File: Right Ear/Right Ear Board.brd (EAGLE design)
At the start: 157.5 x 20.3 mm, 6 parts, among them J1 502585-0470

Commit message: Update right ear boards
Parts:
- removed C2: (no value), rcl:C0402
- added C4: 10uF, rcl:C0603K
- added SV2, SV3: (no value), con-lstb:MA03-1
- C1: value (none) -> 10uF; device rcl:C0402 -> rcl:C0603K
- moved C1 146.6 mm to (3.43, 18.2)
- moved LED7 118.7 mm to (31.8, 16.5), turned to 180 degrees
- moved LED1 7.73 mm to (8.89, 16.5), turned to 180 degrees
- moved SV1 6.93 mm to (9.14, 3.05), flipped to the top, turned to 0 degrees
- moved J1 2.84 mm to (6.35, 11.4), turned to 270 degrees
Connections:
- removed net N$1: LED1.2-DOUT, LED7.4-DIN
- new net DATA: LED1.2-DOUT, LED7.4-DIN, SV2.2, SV3.2
- net +5V: now also C4.1, SV2.1, SV3.3; no longer C2.1
- net GND: now also C4.2, SV2.3, SV3.1; no longer C2.2
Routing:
- net N$1: track 157.1 -> 0.00 mm
- net +5V: track 186.5 -> 50.9 mm
- net GND: track 6.75 -> 61.3 mm, vias 1 -> 2
- net DATA: track 0.00 -> 33.5 mm, vias 0 -> 3
- net DI: track 7.05 -> 16.3 mm
- net SERVO_PWM: track 14.9 -> 12.8 mm, vias 0 -> 1
- removed copper zone on layer 1, net GND
- removed copper zone on layer 16, net GND
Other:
- board size 157.5 x 20.3 mm -> 39.4 x 20.3 mm

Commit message: Made changes
Change LED caps to .1uF on right ear and center
Add resistor to D2
Add level shifters (1 for D1, 1 for D2)
Add mount holes on right ear
Add mosfet for servo (see things to consider.txt)
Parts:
- C1, C4: value 10uF -> .1uF
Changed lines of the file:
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@@
 <?xml version="1.0" encoding="utf-8"?>
 <!DOCTYPE eagle SYSTEM "eagle.dtd">
-<eagle version="8.5.0">
+<eagle version="8.3.1">
 <drawing>
 <settings>
@@
 <param name="dpMaxLengthDifference" value="10mm"/>
 <param name="dpGapFactor" value="2.5"/>
+<param name="checkGrid" value="0"/>
 <param name="checkAngle" value="0"/>
 <param name="checkFont" value="1"/>
 <param name="checkRestrict" value="1"/>
-<param name="checkStop" value="0"/>
-<param name="checkValues" value="0"/>
 <param name="useDiameter" value="13"/>
 <param name="maxErrors" value="50"/>
@@
 <attribute name="VALUE" x="18.161" y="7.62" size="1.27" layer="27" ratio="10" rot="R90"/>
 </element>
-<element name="C4" library="rcl" package="C0603K" value="10uF" x="25.4" y="18.161" smashed="yes" rot="R180">
+<element name="C4" library="rcl" package="C0603K" value=".1uF" x="25.4" y="18.161" smashed="yes" rot="R180">
 <attribute name="NAME" x="26.2" y="17.511" size="1.016" layer="25" rot="R180"/>
 <attribute name="PARTNO" value="GRM188R61A106KE69D" x="25.4" y="18.161" size="1.778" layer="27" rot="R180" display="off"/>
 </element>
-<element name="C1" library="rcl" package="C0603K" value="10uF" x="3.429" y="18.161" smashed="yes" rot="R180">
+<element name="C1" library="rcl" package="C0603K" value=".1uF" x="3.429" y="18.161" smashed="yes" rot="R180">
 <attribute name="NAME" x="4.229" y="17.511" size="1.016" layer="25" rot="R180"/>
 <attribute name="PARTNO" value="GRM188R61A106KE69D" x="3.429" y="18.161" size="1.778" layer="27" rot="R180" display="off"/>

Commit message: Redid right ear board layouts
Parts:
- moved SV1 13.0 mm to (21.6, 6.73), turned to 90 degrees
- moved C1 11.8 mm to (14.4, 13.6), turned to 0 degrees
- moved LED1 8.98 mm to (15.2, 10.2)
- moved C4 8.82 mm to (33.5, 14.7), turned to 0 degrees
- moved LED7 7.04 mm to (34.8, 10.2)
- moved SV3 6.71 mm to (21.6, 13.6)
- moved SV2 5.33 mm to (29.3, 10.3)
- moved J1 1.27 mm to (6.35, 10.2), flipped to the top, turned to 90 degrees
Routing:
- net GND: track 61.3 -> 46.7 mm, vias 2 -> 4
- net DATA: track 33.5 -> 19.4 mm, vias 3 -> 0
- net SERVO_PWM: track 12.8 -> 21.9 mm, vias 1 -> 2
- net +5V: track 50.9 -> 47.3 mm, vias 1 -> 2
- net DI: track 16.3 -> 15.4 mm, vias 1 -> 0
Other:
- board size 39.4 x 20.3 mm -> 40.6 x 20.3 mm

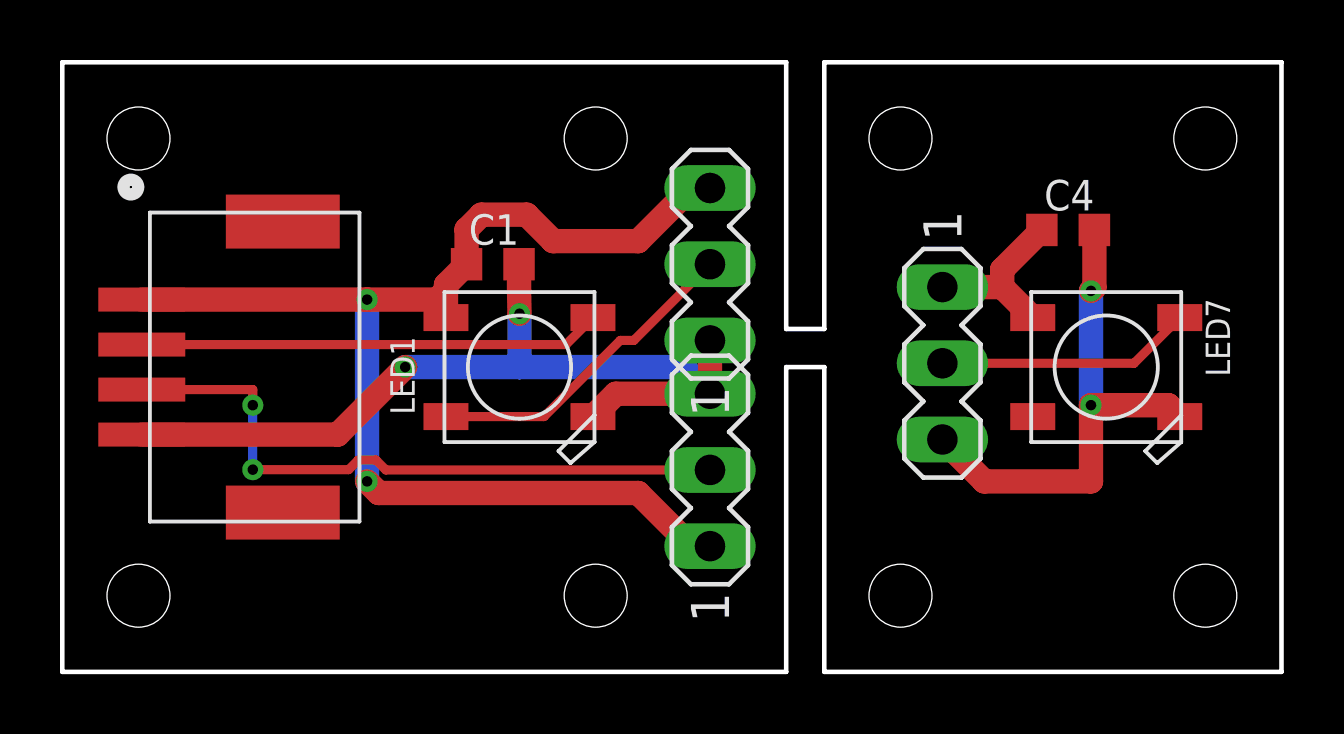
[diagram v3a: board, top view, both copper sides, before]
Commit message: Added level shifter to center dash
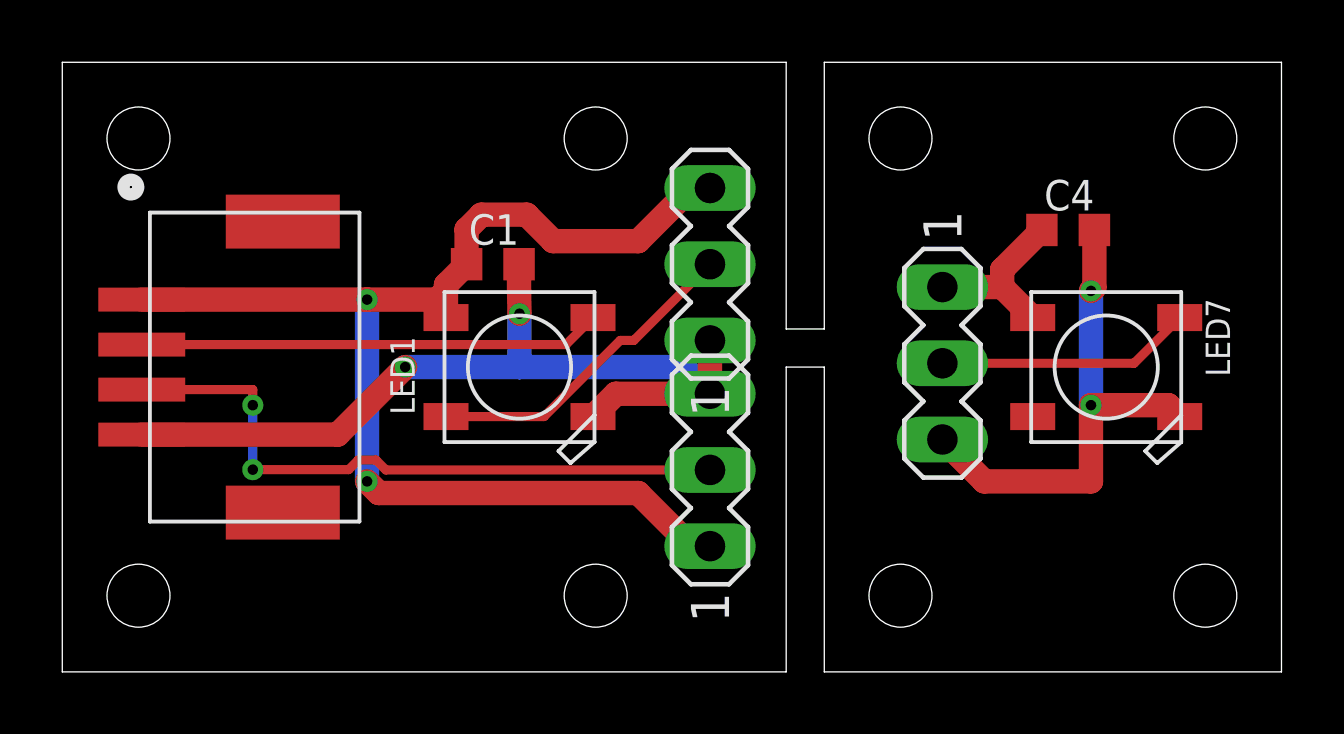
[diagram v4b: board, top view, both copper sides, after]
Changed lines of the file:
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@@
 <setting verticaltext="up"/>
 </settings>
-<grid distance="50" unitdist="mil" unit="mm" style="lines" multiple="1" display="no" altdistance="5" altunitdist="mil" altunit="inch"/>
+<grid distance="50" unitdist="mil" unit="inch" style="lines" multiple="1" display="no" altdistance="5" altunitdist="mil" altunit="inch"/>
 <layers>
 <layer number="1" name="Top" color="4" fill="1" visible="yes" active="yes"/>
@@
 <board>
 <plain>
-<wire x1="40.64" y1="0" x2="40.64" y2="20.32" width="0.1524" layer="20"/>
-<wire x1="0" y1="20.32" x2="0" y2="0" width="0.1524" layer="20"/>
-<wire x1="24.13" y1="11.43" x2="25.4" y2="11.43" width="0.1524" layer="20"/>
-<wire x1="24.13" y1="10.16" x2="25.4" y2="10.16" width="0.1524" layer="20"/>
-<wire x1="0" y1="20.32" x2="24.13" y2="20.32" width="0.1524" layer="20"/>
-<wire x1="24.13" y1="20.32" x2="24.13" y2="11.43" width="0.1524" layer="20"/>
-<wire x1="25.4" y1="11.43" x2="25.4" y2="20.32" width="0.1524" layer="20"/>
-<wire x1="25.4" y1="20.32" x2="40.64" y2="20.32" width="0.1524" layer="20"/>
-<wire x1="25.4" y1="10.16" x2="25.4" y2="0" width="0.1524" layer="20"/>
-<wire x1="25.4" y1="0" x2="40.64" y2="0" width="0.1524" layer="20"/>
-<wire x1="24.13" y1="10.16" x2="24.13" y2="0" width="0.1524" layer="20"/>
-<wire x1="24.13" y1="0" x2="0" y2="0" width="0.1524" layer="20"/>
+<wire x1="40.64" y1="0" x2="40.64" y2="20.32" width="0" layer="20"/>
+<wire x1="0" y1="20.32" x2="0" y2="0" width="0" layer="20"/>
+<wire x1="24.13" y1="11.43" x2="25.4" y2="11.43" width="0" layer="20"/>
+<wire x1="24.13" y1="10.16" x2="25.4" y2="10.16" width="0" layer="20"/>
+<wire x1="0" y1="20.32" x2="24.13" y2="20.32" width="0" layer="20"/>
+<wire x1="24.13" y1="20.32" x2="24.13" y2="11.43" width="0" layer="20"/>
+<wire x1="25.4" y1="11.43" x2="25.4" y2="20.32" width="0" layer="20"/>
+<wire x1="25.4" y1="20.32" x2="40.64" y2="20.32" width="0" layer="20"/>
+<wire x1="25.4" y1="10.16" x2="25.4" y2="0" width="0" layer="20"/>
+<wire x1="25.4" y1="0" x2="40.64" y2="0" width="0" layer="20"/>
+<wire x1="24.13" y1="10.16" x2="24.13" y2="0" width="0" layer="20"/>
+<wire x1="24.13" y1="0" x2="0" y2="0" width="0" layer="20"/>
 <hole x="2.54" y="17.78" drill="2.1"/>
 <hole x="2.54" y="2.54" drill="2.1"/>

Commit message: Done with board layouts
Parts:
- moved LED1 10.2 mm to (5.08, 10.2)
- moved C1 9.79 mm to (4.57, 14.1)
- moved J1 7.75 mm to (14.1, 10.2), turned to 270 degrees
- moved C4 1.27 mm to (34.8, 14.7)
- moved LED7 0.76 mm to (35.6, 10.2)
- moved SV3 0.63 mm to (22.1, 14.0)
- moved SV1 0.51 mm to (22.1, 6.73)
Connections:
- net +5V: now also SV1.2; no longer SV1.1
- net SERVO_PWM: now also SV1.1; no longer SV1.2
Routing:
- net DATA: track 19.4 -> 42.5 mm, vias 0 -> 3
- net SERVO_PWM: track 21.9 -> 9.78 mm, vias 2 -> 1
- net DI: track 15.4 -> 13.2 mm, vias 0 -> 2
- net +5V: track 47.3 -> 49.2 mm, vias 2 -> 3
- net GND: track 46.7 -> 45.6 mm, vias 4 -> 0
